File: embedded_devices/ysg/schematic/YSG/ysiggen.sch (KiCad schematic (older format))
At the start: 2 parts, among them J1 Conn_01x10, U1 ESP32_NODEMCU

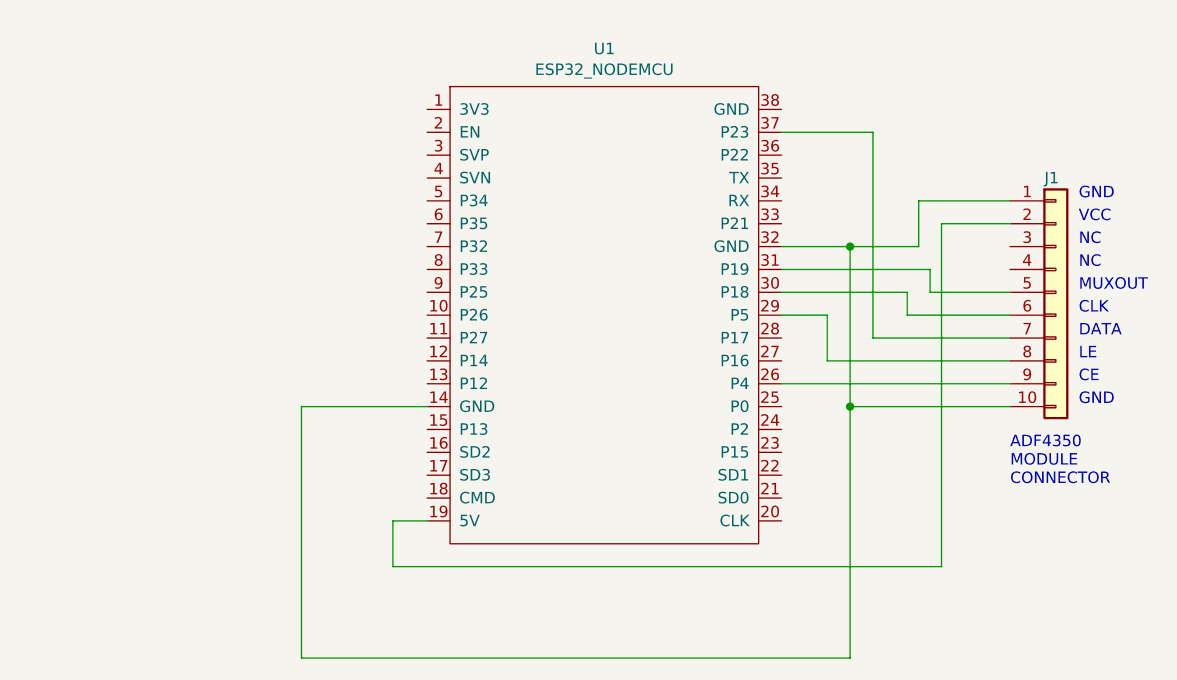
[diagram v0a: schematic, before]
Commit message: - Add ability to calibrate the TX freq. This involved changes to the hardware   and software.   The hardware changes involved changing the TCXO and connecting the TCXO   control voltage to a DAC output on the ESP32 device.   The software changes involved adding a persistently stored cal value and   providing a way (via the ysg.py program) to calibrate the TCXO. - Limit the min TX freq to 138 MHZ rather than 137.5 MHz as some of the lower   frequency harmonics can interfere with the 2.4 GHz WiFi that the device   is controlled over. - Report memory usage every 5 seconds on the serial port as well as via syslog.
Testing was performed with a spectrum analyser to check that the freq accuracy
is now better than 0.5 ppm.
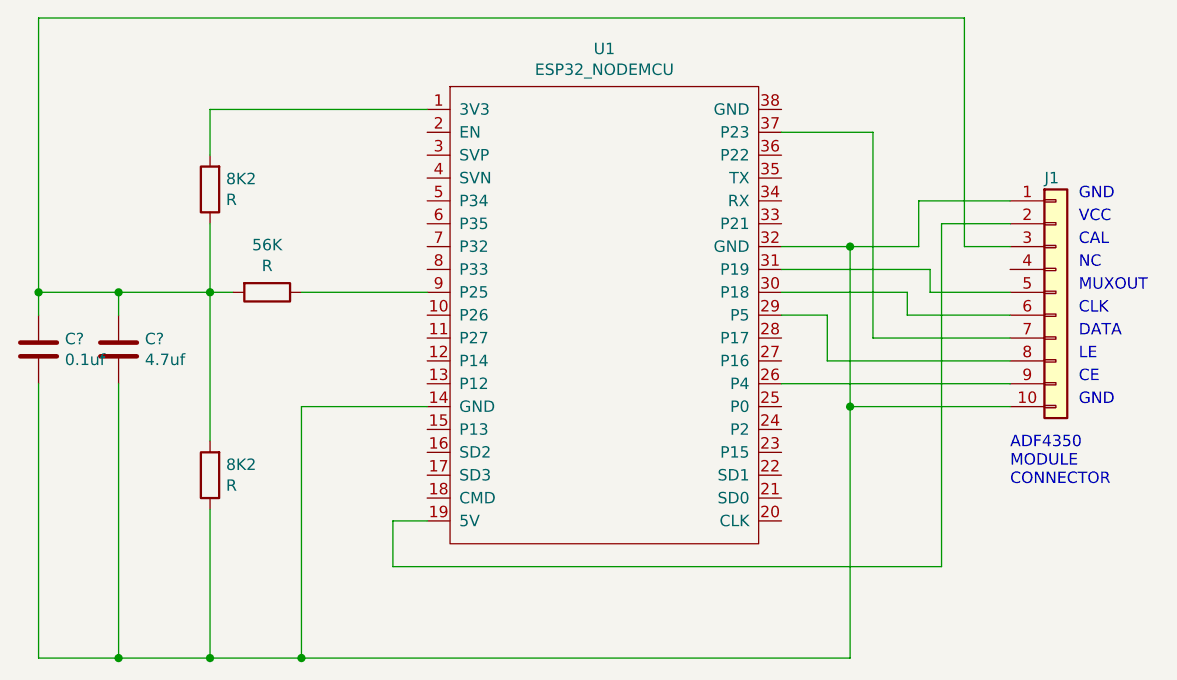
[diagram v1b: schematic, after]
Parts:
- added 56K, 8K2 (x2): R, symbol Device:R
- added C?: 4.7uf, symbol Device:C
- added C?: 0.1uf, symbol Device:C
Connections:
- net at J1.1 (Pin_1), J1.10 (Pin_10), U1.14 (GND)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: now also 8K2.1, C?.2, C?.2
- net at J1.3 (Pin_3): now also 56K.2, 8K2.1, 8K2.2, C?.1, C?.1
- net at U1.1 (3V3): now also 8K2.2
- net at U1.9 (P25): now also 56K.1
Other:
- note added: "CAL"
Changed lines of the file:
@@
 EESchema Schematic File Version 4
+LIBS:ysiggen-cache
 EELAYER 30 0
 EELAYER END
@@
 VCC
 Text Notes 5850 3550 0    50   ~ 0
-NC
+CAL
 Text Notes 5850 3650 0    50   ~ 0
 NC
@@
 Wire Wire Line
 	2450 5350 4850 5350
+Wire Wire Line
+	5550 3550 5350 3550
+$Comp
+L Device:R 56K
+U 1 1 5E1969D5
+P 2300 3750
+F 0 "56K" V 2093 3750 50  0000 C CNN
+F 1 "R" V 2184 3750 50  0000 C CNN
+F 2 "" V 2230 3750 50  0001 C CNN
+F 3 "~" H 2300 3750 50  0001 C CNN
+	1    2300 3750
+	0    1    1    0
+$EndComp
+Wire Wire Line
+	2450 3750 3000 3750
+Connection ~ 2450 5350
+$Comp
+L Device:C C?
+U 1 1 5E198E79
+P 1650 4000
+F 0 "C?" H 1765 4046 50  0000 L CNN
+F 1 "4.7uf" H 1765 3955 50  0000 L CNN
+F 2 "" H 1688 3850 50  0001 C CNN
+F 3 "~" H 1650 4000 50  0001 C CNN
+	1    1650 4000
+	1    0    0    -1
+$EndComp
+$Comp
+L Device:C C?
+U 1 1 5E199144
+P 1300 4000
+F 0 "C?" H 1415 4046 50  0000 L CNN
+F 1 "0.1uf" H 1415 3955 50  0000 L CNN
+F 2 "" H 1338 3850 50  0001 C CNN
+F 3 "~" H 1300 4000 50  0001 C CNN
+	1    1300 4000
+	1    0    0    -1
+$EndComp
+Wire Wire Line
+	1650 3750 1650 3850
+Wire Wire Line
+	1650 3750 1300 3750
+Wire Wire Line
+	1300 3750 1300 3850
+Connection ~ 1650 3750
+Wire Wire Line
+	1300 4150 1300 5350
+Wire Wire Line
+	1300 5350 1650 5350
+Wire Wire Line
+	1650 4150 1650 5350
+Connection ~ 1650 5350
+Wire Wire Line
+	5350 3550 5350 2550
+Wire Wire Line
+	5350 2550 1300 2550
+Wire Wire Line
+	1300 2550 1300 3750
+Connection ~ 1300 3750
+Wire Wire Line
+	1650 3750 2050 3750
+$Comp
+L Device:R 8K2
+U 1 1 5E19DF5B
+P 2050 3300
+F 0 "8K2" H 1980 3254 50  0000 R CNN
+F 1 "R" H 1980 3345 50  0000 R CNN
+F 2 "" V 1980 3300 50  0001 C CNN
+F 3 "~" H 2050 3300 50  0001 C CNN
+	1    2050 3300
+	-1   0    0    1
+$EndComp
+$Comp
+L Device:R 8K2
+U 1 1 5E19E5F7
+P 2050 4550
+F 0 "8K2" H 1980 4504 50  0000 R CNN
+F 1 "R" H 1980 4595 50  0000 R CNN
+F 2 "" V 1980 4550 50  0001 C CNN
+F 3 "~" H 2050 4550 50  0001 C CNN
+	1    2050 4550
+	-1   0    0    1
+$EndComp
+Wire Wire Line
+	3000 2950 2050 2950
+Wire Wire Line
+	2050 2950 2050 3150
+Wire Wire Line
+	2050 3450 2050 3750
+Connection ~ 2050 3750
+Wire Wire Line
+	2050 3750 2150 3750
+Wire Wire Line
+	2050 3750 2050 4400
+Wire Wire Line
+	2050 4700 2050 5350
+Wire Wire Line
+	1650 5350 2050 5350
+Connection ~ 2050 5350
+Wire Wire Line
+	2050 5350 2450 5350
 $EndSCHEMATC

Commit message: Add the latest schematic of the YView siggen embedded device.
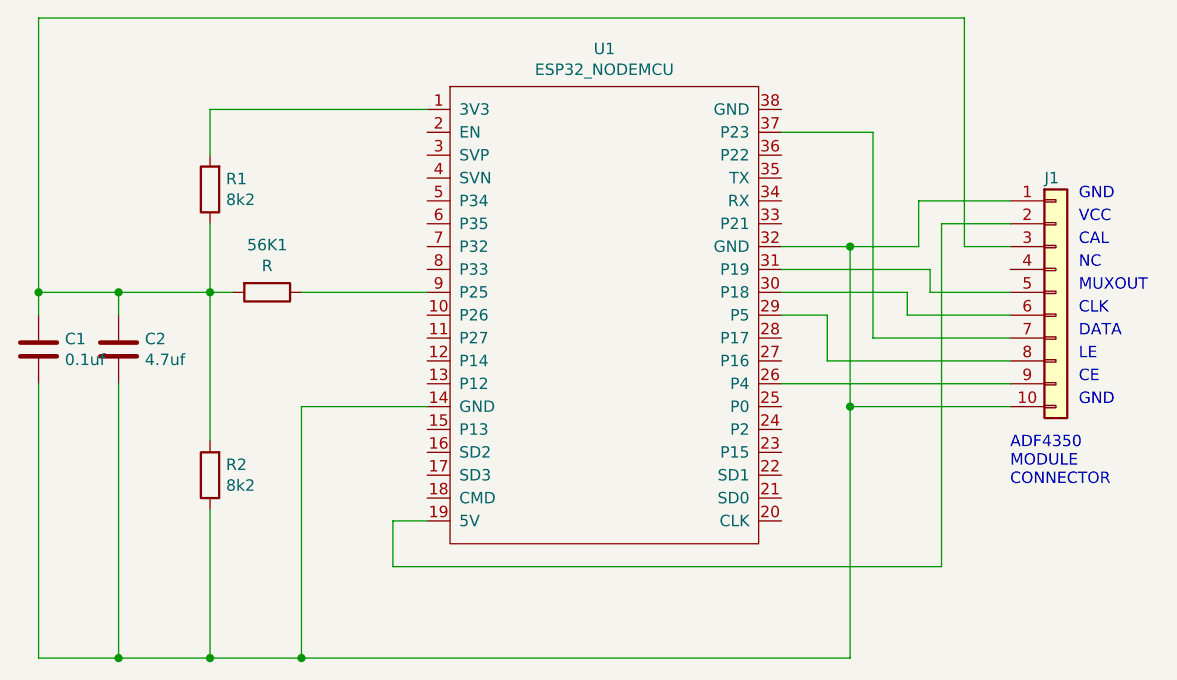
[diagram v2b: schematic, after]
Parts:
- R1, R2: renamed from 8K2; value R -> 8k2
- gave numbers to parts that had none: 2
- renumbered 56K to 56K1
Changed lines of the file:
@@
 EESchema Schematic File Version 4
-LIBS:ysiggen-cache
 EELAYER 30 0
 EELAYER END
@@
 	5550 3550 5350 3550
 $Comp
-L Device:R 56K
+L Device:R 56K1
 U 1 1 5E1969D5
 P 2300 3750
-F 0 "56K" V 2093 3750 50  0000 C CNN
+F 0 "56K1" V 2093 3750 50  0000 C CNN
 F 1 "R" V 2184 3750 50  0000 C CNN
 F 2 "" V 2230 3750 50  0001 C CNN
@@
 Connection ~ 2450 5350
 $Comp
-L Device:C C?
+L Device:C C2
 U 1 1 5E198E79
 P 1650 4000
-F 0 "C?" H 1765 4046 50  0000 L CNN
+F 0 "C2" H 1765 4046 50  0000 L CNN
 F 1 "4.7uf" H 1765 3955 50  0000 L CNN
 F 2 "" H 1688 3850 50  0001 C CNN
@@
 $EndComp
 $Comp
-L Device:C C?
+L Device:C C1
 U 1 1 5E199144
 P 1300 4000
-F 0 "C?" H 1415 4046 50  0000 L CNN
+F 0 "C1" H 1415 4046 50  0000 L CNN
 F 1 "0.1uf" H 1415 3955 50  0000 L CNN
 F 2 "" H 1338 3850 50  0001 C CNN
@@
 	1650 3750 2050 3750
 $Comp
-L Device:R 8K2
+L Device:R R1
 U 1 1 5E19DF5B
 P 2050 3300
-F 0 "8K2" H 1980 3254 50  0000 R CNN
-F 1 "R" H 1980 3345 50  0000 R CNN
+F 0 "R1" H 1980 3254 50  0000 R CNN
+F 1 "8k2" H 1980 3345 50  0000 R CNN
 F 2 "" V 1980 3300 50  0001 C CNN
 F 3 "~" H 2050 3300 50  0001 C CNN
@@
 $EndComp
 $Comp
-L Device:R 8K2
+L Device:R R2
 U 1 1 5E19E5F7
 P 2050 4550
-F 0 "8K2" H 1980 4504 50  0000 R CNN
-F 1 "R" H 1980 4595 50  0000 R CNN
+F 0 "R2" H 1980 4504 50  0000 R CNN
+F 1 "8k2" H 1980 4595 50  0000 R CNN
 F 2 "" V 1980 4550 50  0001 C CNN
 F 3 "~" H 2050 4550 50  0001 C CNN
